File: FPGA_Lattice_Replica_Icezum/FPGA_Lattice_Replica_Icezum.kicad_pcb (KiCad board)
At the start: 4 copper layers, 200 parts, among them J1 USB_Micro_Type_B, J10 1x8_male_pin_Header_2.54mm, J11 1x6_female_pin_Header_2.54mm, J12 1x6_female_pin_Header_2.54mm, J13 1x6_female_pin_Header_2.54mm, J14 1x6_female_pin_Header_2.54mm, J15 1x4_male_pin_Header_2.54mm, J16 1x4_male_pin_Header_2.54mm, J17 1x4_male_pin_Header_2.54mm, J18 Power_Jack, J19 2x4_male_pin_Header_2.54mm, J2 1x6_female_pin_Header_2.54mm, J3 1x6_female_pin_Header_2.54mm, J4 1x10_female_pin_Header_2.54mm, J5 1x8_male_pin_Header_2.54mm, J6 1x6_female_pin_Header_2.54mm, J7 1x8_male_pin_Header_2.54mm, J8 1x8_male_pin_Header_2.54mm, J9 1x8_male_pin_Header_2.54mm, Q1 DMP3017, Q2 DMP3017, Q3 DMP2035U-7, Q4 Mosfet_P_DFN-6, Q5 PMBT3906, SW1 SW1, SW2 Switch_4p, SW3 SPDT_Switch, SW4 Switch, U1 iCE40HX1K-TQ144, U10 AP7361, U11 TLV711, U12 TPS62133RGTR, U13 APX810, U2 N25Q032A, U3 FT2232H, U4 DSC1001, U5 93LC56C, U6 TXB0106, U7 ADS7924, U8 TXB0108, U9 TXB0108

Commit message: se comenzo PCB terminado ordenamiento y borde de placa
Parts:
- moved R30 458.3 mm to (147.8, 118.3), turned to 270 degrees
- moved U12 453.9 mm to (134.2, 104.0)
- moved C59 453.7 mm to (142.1, 124.1)
- moved C61 452.1 mm to (155.0, 110.2), turned to 270 degrees
- moved C66 451.7 mm to (142.5, 94.0), turned to 180 degrees
- moved C64 449.0 mm to (162.1, 117.4), turned to 270 degrees
- moved TP4 448.4 mm to (135.2, 125.5)
- moved J18 447.0 mm to (129.7, 114.0)
- moved Q4 446.2 mm to (139.9, 104.0), turned to 270 degrees
- moved C62 446.2 mm to (158.1, 115.3), turned to 180 degrees
- moved R27 445.2 mm to (154.7, 115.7), turned to 90 degrees
- moved Q2 445.1 mm to (161.4, 108.9), turned to 90 degrees
- moved C71 444.0 mm to (145.3, 104.3)
- moved Q1 443.9 mm to (149.4, 105.9), turned to 180 degrees
- moved C65 442.8 mm to (156.4, 117.4), turned to 270 degrees
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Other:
- board outline added: 78.8 x 79.3 mm

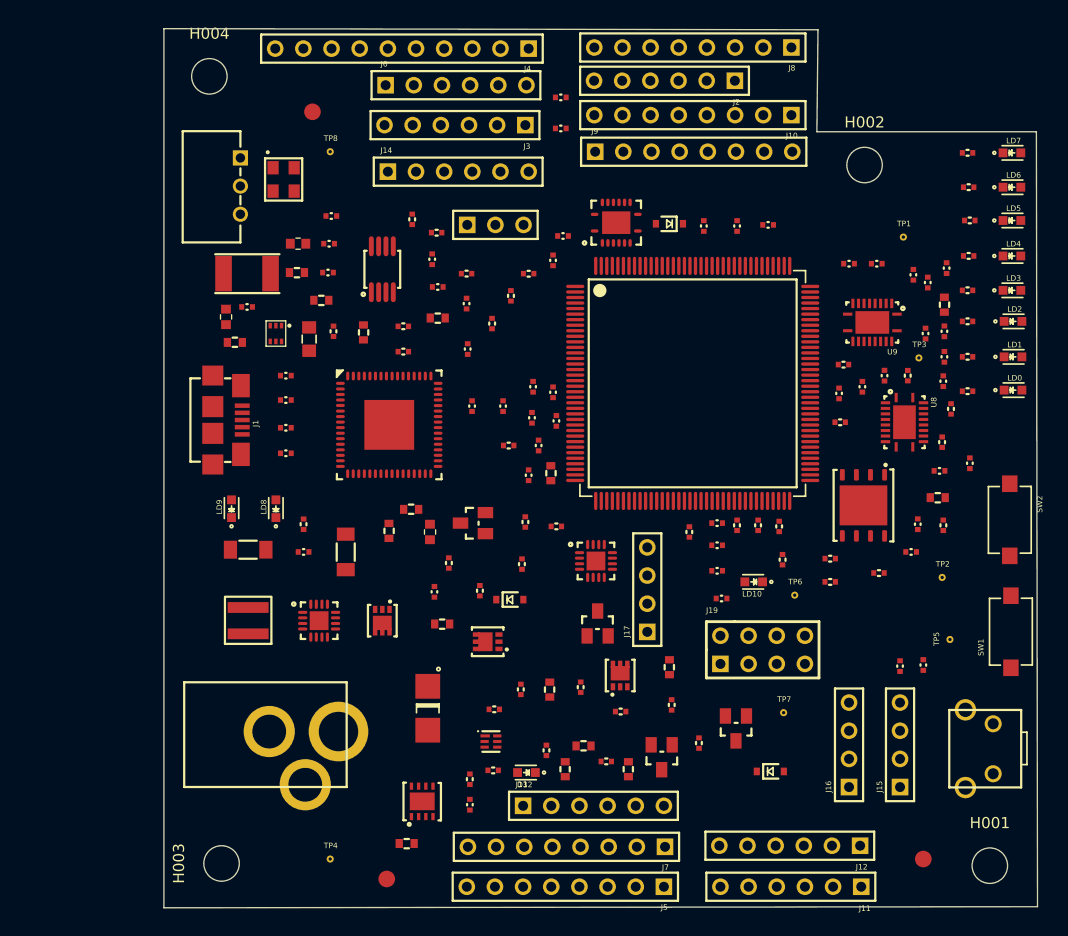
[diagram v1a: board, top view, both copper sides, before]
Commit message: se mejoro esquematico de acuerdo a la revisión del docente. Se mejoro rotulo (se coloco link del repo, autor y autor de la versión original y la licencia) se mejoro el flujo izquiera derecha de los botones, se desplazo fiduciales a la página principal, se achico el esquematico en la parte de headers
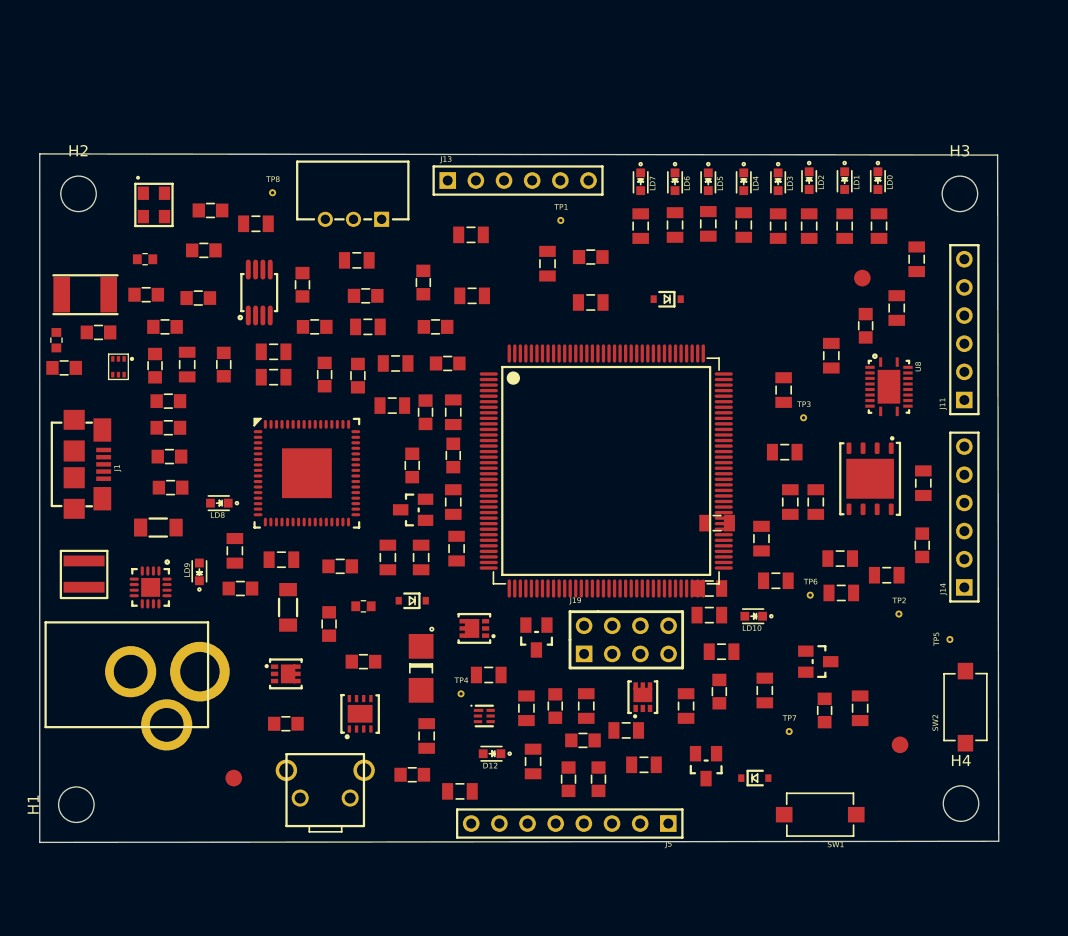
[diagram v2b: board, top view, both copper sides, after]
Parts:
- removed C36, C37, C45, C46, C50: 100 nF, footprints:C_0402
- removed C38, C39, C40, C42, C43, C44, C51, C52, C53, C54, C55, C56, C57, C58: 100 pF, footprints:C_0402
- removed C41: 4.7 uF, footprints:C_0603
- removed C49: 100 nF, footprints:C_0603
- removed H001, H002, H003, H004: MountingHole, MountingHole:MountingHole_3.2mm_M3_ISO7380
- removed J10, J7, J8, J9: 1x8_male_pin_Header_2.54mm, footprints:1x8_Socket_header_2.54mm
- removed J12, J2, J3, J6: 1x6_female_pin_Header_2.54mm, footprints:1x6-pin-header-2.54mm
- removed J15, J16, J17: 1x4_male_pin_Header_2.54mm, footprints:1x04-pin-header-2.54mm
- removed J4: 1x10_female_pin_Header_2.54mm, footprints:1x10_socket-header-2.54mm
- removed JP1: Jumper_3pin, footprints:1x03-pin-header-2.54mm
- removed R19, R20, R21: 10K±5% 0.063W, footprints:R_0402
- removed U6: TXB0106, footprints:VQFN16
- removed U7: ADS7924, footprints:QFN16
- removed U9: TXB0108, footprints:VQFN20
- added H1: MountingHole, MountingHole:MountingHole_3.2mm_M3_ISO7380, F.Cu at (112.3, 120.6)
- added H2: MountingHole, MountingHole:MountingHole_3.2mm_M3_ISO7380, F.Cu at (112.5, 65.5)
- added H3: MountingHole, MountingHole:MountingHole_3.2mm_M3_ISO7380, F.Cu at (192.0, 65.5)
- added H4: MountingHole, MountingHole:MountingHole_3.2mm_M3_ISO7380, F.Cu at (192.1, 120.5)
- C1, C10, C2, C3, C4, C5, C6, C7, C8, C9: footprint footprints:C_0402 -> footprints:F_0805
- C11, C17, C22, C24, C31, C32, C59, C60, C61, C62, C64, C65, C66, C70, C71: footprint footprints:C_0603 -> footprints:L_0805
- C12, C13, C14, C15, C16, C18, C19, C20, C21, C23, C25, C26, C27, C28, C29, C30, C33, C34, C35, C47, C48, C63, C68: footprint footprints:C_0402 -> footprints:L_0805
- R1, R10, R11, R12, R13, R14, R15, R16, R17, R18, R2, R22, R23, R24, R25, R26, R27, R28, R29, R3, R30, R31, R32, R33, R34, R35, R36, R37, R38, R39, R4, R40, R41, R42, R43, R44, R45, R46, R47, R48, R5, R6, R7, R8, R9: footprint footprints:R_0402 -> footprints:F_0805
- moved J14 64.1 mm to (192.4, 101.0), turned to 90 degrees
- moved FID1 60.5 mm to (126.5, 118.2)
- moved SW4 58.4 mm to (137.0, 120.0), turned to 270 degrees
- moved J13 56.8 mm to (145.8, 64.3)
- moved FID3 52.7 mm to (183.2, 73.1)
- moved FID2 47.9 mm to (186.6, 115.2)
- moved J11 44.9 mm to (192.4, 84.1), turned to 90 degrees
- moved R1 36.9 mm to (130.8, 98.5), turned to 180 degrees
- moved LD7 33.6 mm to (163.2, 64.4), turned to 270 degrees
- moved TP1 30.9 mm to (156.0, 67.9)
- moved LD6 30.4 mm to (166.3, 64.4), turned to 270 degrees
- moved R45 30.2 mm to (163.2, 68.4), turned to 270 degrees
- moved LD5 27.6 mm to (169.3, 64.4), turned to 270 degrees
- moved R44 26.7 mm to (166.3, 68.3), turned to 270 degrees
- moved LD4 25.1 mm to (172.5, 64.4), turned to 270 degrees
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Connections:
- SW1 pad 1: U_SW1 -> +3V3
- SW1 pad 2: +3V3 -> U_SW1
- SW2 pad 1: U_SW2 -> +3V3
- SW2 pad 2: +3V3 -> U_SW2
- U1 pad 112: FPGA_112_IO_PIN -> Net-(U1-Pad112)
- U1 pad 113: FPGA_113_IO_PIN -> Net-(U1-Pad113)
- U1 pad 114: FPGA_114_IO_PIN -> Net-(U1-Pad114)
- U1 pad 115: FPGA_115_IO_PIN -> Net-(U1-Pad115)
- U1 pad 116: FPGA_116_IO_PIN -> Net-(U1-Pad116)
- U1 pad 117: FPGA_117_IO_PIN -> Net-(U1-Pad117)
- U1 pad 118: FPGA_118_IO_PIN -> Net-(U1-Pad118)
- U1 pad 119: FPGA_119_IO_PIN -> Net-(U1-Pad119)
- U1 pad 138: FPGA_138_IO_PIN -> Net-(U1-Pad138)
- U1 pad 139: FPGA_139_IO_PIN -> Net-(U1-Pad139)
- U1 pad 141: FPGA_141_IO_PIN -> Net-(U1-Pad141)
- U1 pad 142: FPGA_142_IO_PIN -> Net-(U1-Pad142)
- U1 pad 143: FPGA_143_IO_PIN -> Net-(U1-Pad143)
- U1 pad 144: FPGA_144_IO_PIN -> Net-(U1-Pad144)
- U1 pad 90: ADC_SDA -> Net-(U1-Pad90)
- U1 pad 91: ADC_SCL -> Net-(U1-Pad91)
- U1 pad 93: ADC_INT -> Net-(U1-Pad93)
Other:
- board size 78.8 x 79.3 mm -> 86.5 x 62.1 mm

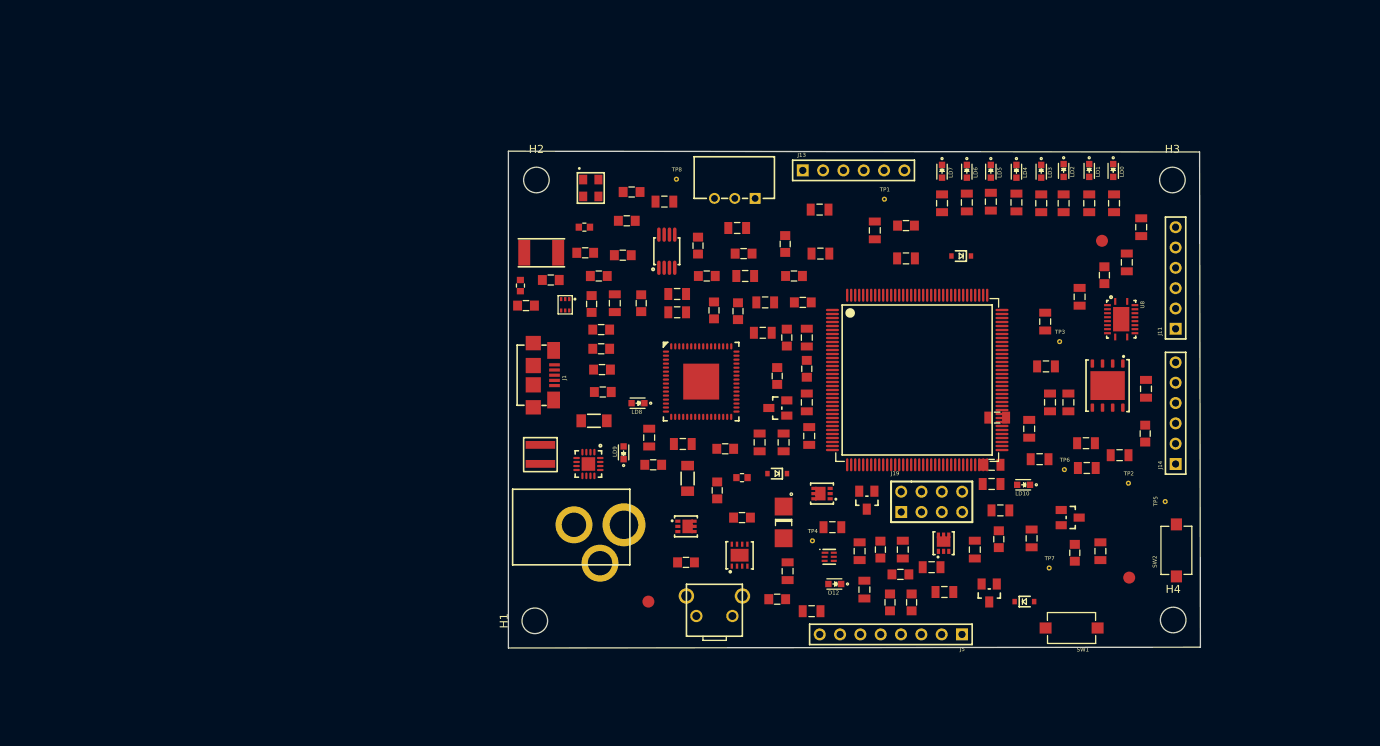
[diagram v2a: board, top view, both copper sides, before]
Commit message: Posicionamiento y PCB finalizado al 90% realizado en 4 capas. Relleno ce Cu
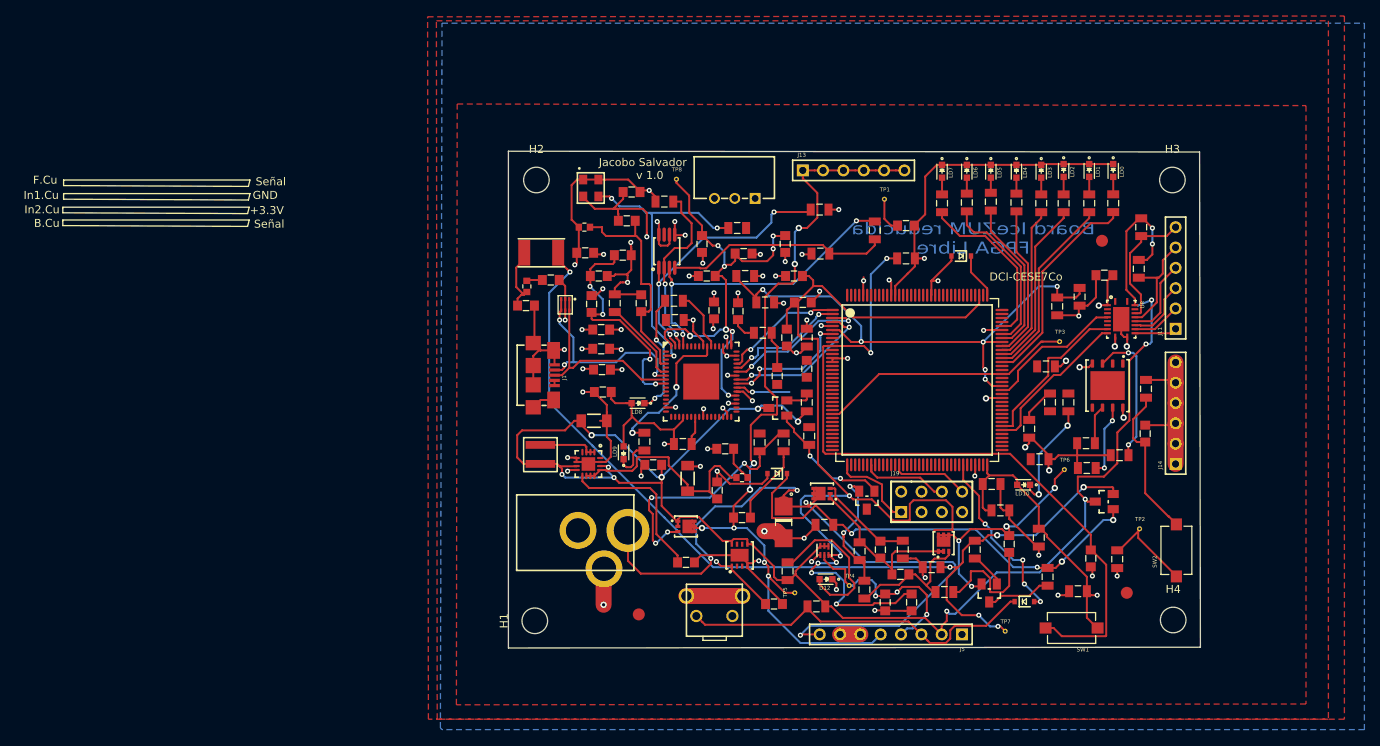
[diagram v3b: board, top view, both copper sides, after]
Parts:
- moved TP5 47.7 mm to (144.8, 117.1)
- moved C1 23.9 mm to (180.2, 116.9), turned to 180 degrees
- moved C2 10.8 mm to (175.3, 110.2), turned to 270 degrees
- moved TP7 9.63 mm to (171.1, 121.9)
- moved TP4 7.25 mm to (151.6, 116.2)
- moved TP2 5.87 mm to (187.9, 109.1)
- moved R28 5.20 mm to (176.4, 115.1)
- moved Q3 4.92 mm to (183.6, 105.7), turned to 90 degrees
- moved C5 2.42 mm to (177.6, 81.3)
- moved C4 2.33 mm to (185.1, 112.9)
- moved C34 2.12 mm to (181.8, 112.8)
- moved FID1 2.00 mm to (125.3, 119.8)
- moved FID2 1.92 mm to (186.3, 117.1)
- moved R23 1.70 mm to (187.8, 76.6)
- moved C60 1.43 mm to (171.6, 111.0)
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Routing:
- net GND: track 0.00 -> 266.9 mm, vias 0 -> 56
- net +5V: track 0.00 -> 218.1 mm, vias 0 -> 13
- net +3V3: track 0.00 -> 160.9 mm, vias 0 -> 25
- net +1V2: track 0.00 -> 158.1 mm, vias 0 -> 6
- net USB_5V: track 0.00 -> 121.1 mm, vias 0 -> 6
- net +5V_P: track 0.00 -> 106.7 mm, vias 0 -> 8
- net Power: track 0.00 -> 100.3 mm, vias 0 -> 10
- net VIN: track 0.00 -> 95.3 mm, vias 0 -> 4
- net U_SW1: track 0.00 -> 92.6 mm, vias 0 -> 2
- net +1V8_FT: track 0.00 -> 59.2 mm, vias 0 -> 8
- net Net-(D2-Pad1): track 0.00 -> 57.3 mm, vias 0 -> 4
- net SYS_RESET: track 0.00 -> 45.9 mm
- net /USB_communication/FT_DATA: track 0.00 -> 39.5 mm, vias 0 -> 3
- net Net-(R16-Pad1): track 0.00 -> 38.0 mm, vias 0 -> 3
- net /USB_communication/FT_CS: track 0.00 -> 33.8 mm, vias 0 -> 3
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- added copper zone on B.Cu, net (none)
- added copper zone on F.Cu, net (none)
- added copper zone on In2.Cu, net +3V3
- added copper zone on In1.Cu, net GND
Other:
- board text added: "+3.3V"
- board text added: "B.Cu"
- board text added: "Board IceZUM reducida FPGA Libre"
- board text added: "DCI-CESE7Co"
- board text added: "F.Cu"
- board text added: "GND"
- board text added: "In1.Cu"
- board text added: "In2.Cu"
- board text added: "Jacobo Salvador v 1.0"
- board text added: "Notas: modelo de 4 capas capas externas: señales capas internas: In1.Cu: GND In2.Cu:+3.3V Ancho de pista: 0.254 mm vías 0.64 / 0.3 mm Superfie rectangular 86.4 x 61.9 mm"
- board text added: "Señal"

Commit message: nota para fabricante, serigrafia y logo open source. PCB finalizado para presentar
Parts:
- added G***: LOGO, footprints:logo, F.Cu at (117.3, 119.9)
- TP4: value TestPoint_Small -> TestPoint
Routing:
- net Power: track 100.3 -> 119.7 mm, vias 10 -> 12
- net FPGA_039_IO_PIN: track 0.00 -> 19.3 mm, vias 0 -> 2
- net FT_RX: track 6.86 -> 21.1 mm, vias 1 -> 2
- net U_SW1: track 92.6 -> 79.7 mm, vias 2 -> 4
- net Net-(C11-Pad1): track 4.71 -> 9.39 mm
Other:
- board text added: "Nota para fabricante Terminación HALS"
- board text added: "Notas: modelo de 4 capas capas externas: señales capas internas: In1.Cu: GND In2.Cu:+3.3V ------------- Grilla: 0.1 mm Ancho de pista: 0.254 mm vías 0.64 / 0.3 mm ------------- Superfie rectangular 86.4 x 61.9 mm"
- board text added: "Power Jack"
- board text added: "SW1"
- board text added: "SW2"
- board text added: "SW4"
- board text added: "Stackup"
- board text added: "TPS62133"
- board text added: "https://github.com/FPGAwars/icezum.git"
- board text added: "iCE40HX1K"
- board text added: "micro USB"
- board text removed: "Notas: modelo de 4 capas capas externas: señales capas internas: In1.Cu: GND In2.Cu:+3.3V Ancho de pista: 0.254 mm vías 0.64 / 0.3 mm Superfie rectangular 86.4 x 61.9 mm"
